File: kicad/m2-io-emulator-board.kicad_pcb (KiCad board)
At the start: 2 copper layers, 180 x 190 mm, 119 parts, among them J1 N2550-6002-RB, J10 61300811121, J11 61301011121, J12 Pin Header 02x18 2.54mm Verti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, J13 VGA femelle, J14 VIDEO, J2 N2526-6002-RB, J3 B10P-SHF-1AA, J4 B12P-SHF-1AA, J5 B12P-SHF-1AA, J6 61300811121, J7 61300811121, J8 61300811121, J9 61300811121, SW1 TEST, SW2 SERVICE, U2 74HCT86, U3 OPA3355EA

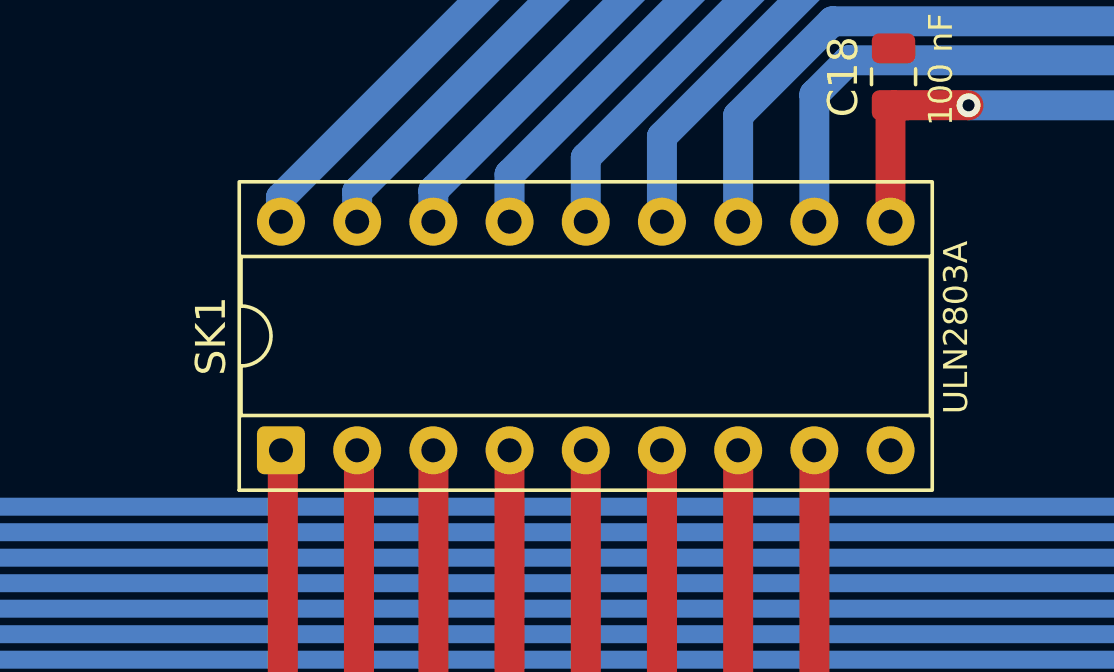
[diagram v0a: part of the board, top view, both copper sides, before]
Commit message: U1 (ULN2803A) soldered directly: DIP-18 socket SK1 removed from schematic, PCB and BOM; Gerbers (silkscreen only), schematic PDF and renders updated
Co-Authored-By: Claude Opus 5.5 <noreply@anthropic.com>
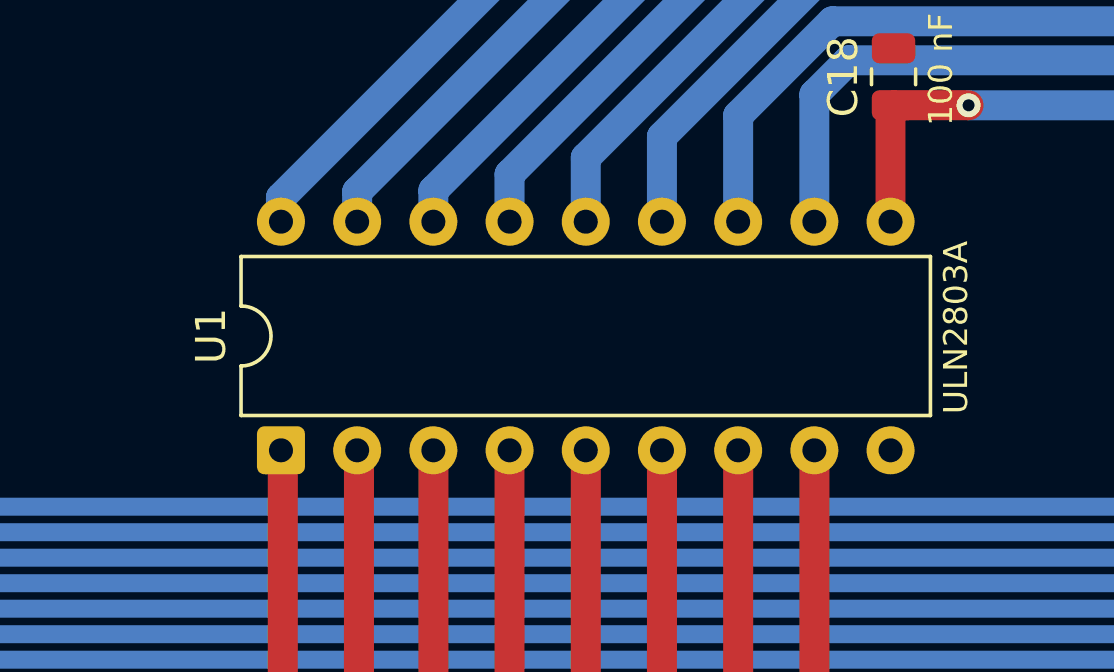
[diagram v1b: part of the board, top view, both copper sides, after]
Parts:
- removed SK1: 1-2199298-5, Package_DIP:DIP-18_W7.62mm_Socket
- added U1: ULN2803A, Package_DIP:DIP-18_W7.62mm, F.Cu at (68.7, 34.6)

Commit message: V2: screen jumper JP8 (Mega D36 to ground: ON = CRT 4:3, OFF = LVDS 16:9), framed silkscreen; Gerbers, drill files, schematic PDF, renders and BOM (EN/FR) updated
V1, the board ordered from JLCPCB on 2026-10-13, is tagged v1. JLCPCB BOM and CPL are unchanged (JP8 is through-hole).

Co-Authored-By: Claude Opus 5.5 <noreply@anthropic.com>
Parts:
- added JP8: 61300211121, Connector_PinHeader_2.54mm:PinHeader_1x02_P2.54mm_Vertical, F.Cu at (80.0, 118.0)
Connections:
- J12 pad 18: unconnected-(J12-Pin_17-Pad18) -> /MEGA_D36_ECRAN
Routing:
- net /MEGA_D36_ECRAN: track 0.00 -> 50.4 mm, vias 0 -> 1
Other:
- board text added: "OFF = LVDS 16:9"
- board text added: "ON = CRT (4:3)"
- board text added: "SCREEN"

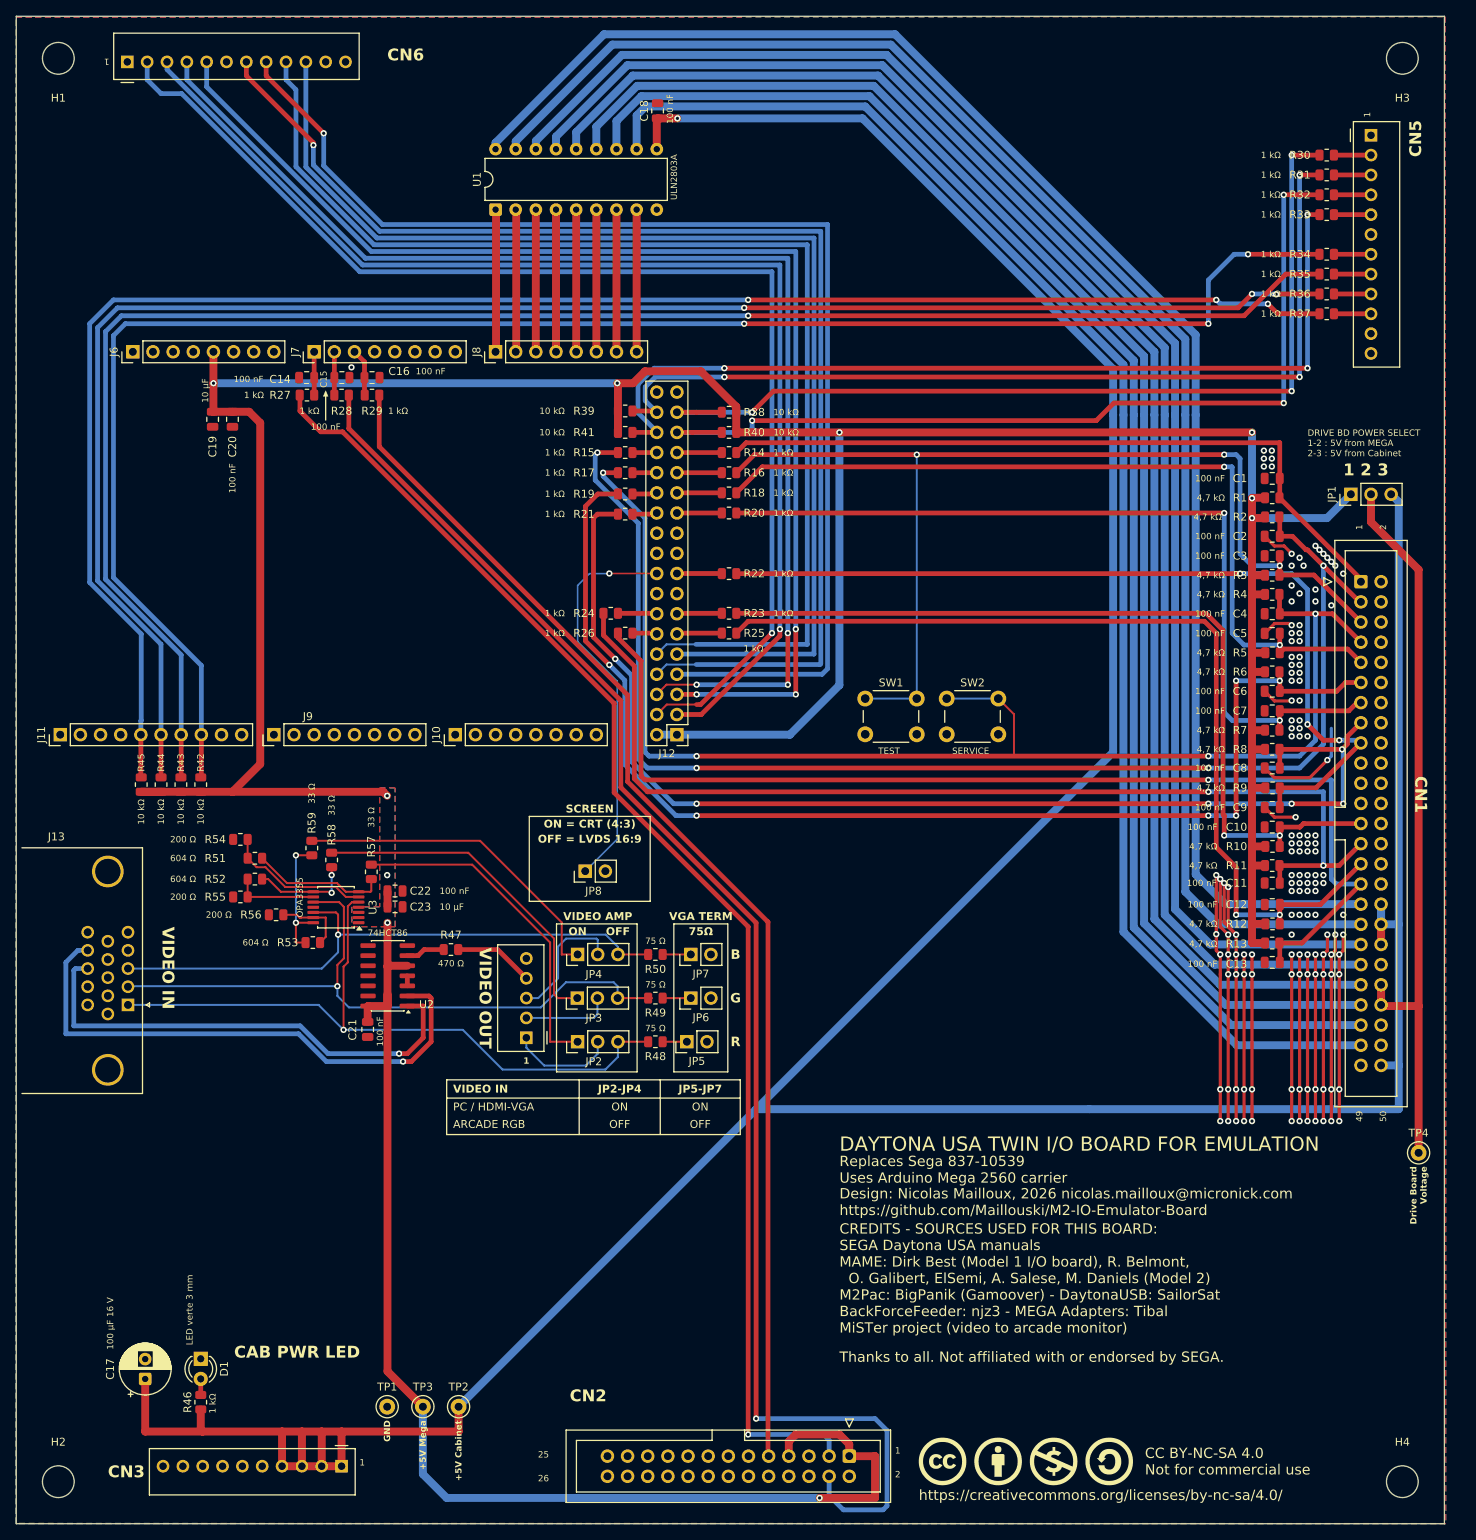
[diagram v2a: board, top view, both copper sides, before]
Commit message: V3: HDMI input with on-board HDMI to VGA converter (CS5213), source jumper JP9, converter power jumper JP10, stereo RCA output, optional EDID EEPROM (DNP); Gerbers, drill files, schematic PDF, renders, BOM (EN/FR) and JLCPCB files updated
Co-Authored-By: Claude Opus 5.5 <noreply@anthropic.com>
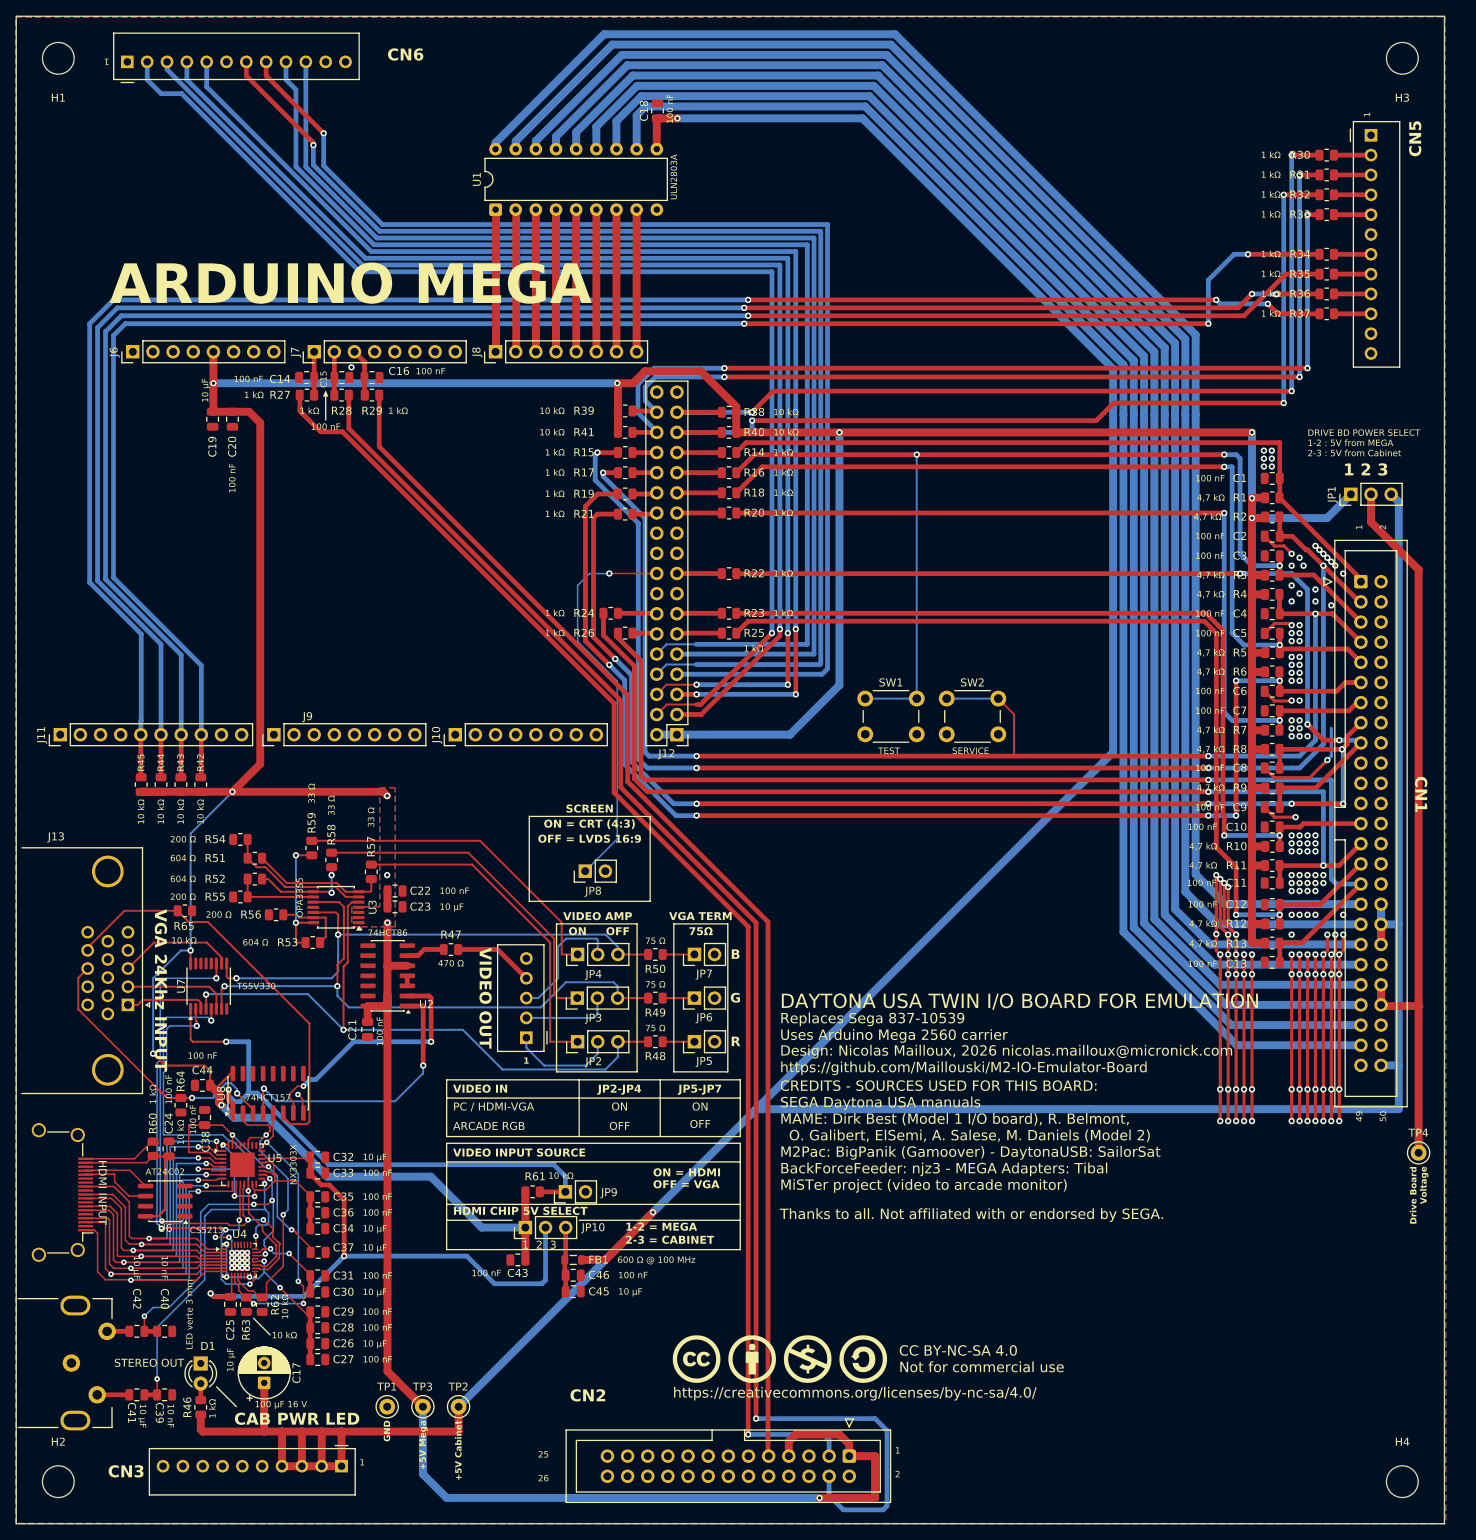
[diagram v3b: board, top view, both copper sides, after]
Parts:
- added C24: 100 nF, Capacitor_SMD:C_0805_2012Metric, F.Cu at (27.5, 153.0)
- added C25: 10 µF, Capacitor_SMD:C_0805_2012Metric, F.Cu at (35.2, 172.6)
- added C26: 10 µF, Capacitor_SMD:C_0805_2012Metric, F.Cu at (46.2, 177.6)
- added C27: 100 nF, Capacitor_SMD:C_0805_2012Metric, F.Cu at (46.2, 179.6)
- added C28: 100 nF, Capacitor_SMD:C_0805_2012Metric, F.Cu at (46.2, 175.6)
- added C29: 100 nF, Capacitor_SMD:C_0805_2012Metric, F.Cu at (46.2, 173.6)
- added C30: 10 µF, Capacitor_SMD:C_0805_2012Metric, F.Cu at (46.2, 171.1)
- added C31: 100 nF, Capacitor_SMD:C_0805_2012Metric, F.Cu at (46.2, 169.0)
- added C32: 10 µF, Capacitor_SMD:C_0805_2012Metric, F.Cu at (46.2, 154.1)
- added C33: 100 nF, Capacitor_SMD:C_0805_2012Metric, F.Cu at (46.2, 156.1)
- added C34: 10 µF, Capacitor_SMD:C_0805_2012Metric, F.Cu at (46.2, 163.1)
- added C35: 100 nF, Capacitor_SMD:C_0805_2012Metric, F.Cu at (46.2, 159.1)
- added C36: 100 nF, Capacitor_SMD:C_0805_2012Metric, F.Cu at (46.2, 161.1)
- added C37: 10 µF, Capacitor_SMD:C_0805_2012Metric, F.Cu at (46.3, 166.1)
- added C38: 100 nF, Capacitor_SMD:C_0805_2012Metric, F.Cu at (32.0, 149.1)
- added C39: 10 nF, Capacitor_SMD:C_0805_2012Metric, F.Cu at (26.9, 184.0)
- added C40: 10 nF, Capacitor_SMD:C_0805_2012Metric, F.Cu at (26.9, 176.0)
- added C41: 10 µF, Capacitor_SMD:C_0805_2012Metric, F.Cu at (23.4, 184.0)
- added C42: 10 µF, Capacitor_SMD:C_0805_2012Metric, F.Cu at (23.4, 176.0)
- added C43: 100 nF, Capacitor_SMD:C_0805_2012Metric, F.Cu at (71.5, 167.0)
- added C44: 100 nF, Capacitor_SMD:C_0805_2012Metric, F.Cu at (31.7, 145.0)
- added C45: 10 µF, Capacitor_SMD:C_0805_2012Metric, F.Cu at (78.5, 171.0)
- added C46: 100 nF, Capacitor_SMD:C_0805_2012Metric, F.Cu at (78.5, 168.9)
- added FB1: 600 Ω @ 100 MHz, Inductor_SMD:L_0805_2012Metric, F.Cu at (78.5, 167.0)
- added J15: HDMI A, Connector_Video:HDMI_A_Amphenol_10029449-x01xLF_Horizontal, F.Cu at (12.0, 158.5)
- added J16: RCJ-2223, interface-borne:CUI_RCJ-22xx_RCA_Dual_Horizontal, F.Cu at (8.20, 180.0)
- added JP10: 61300311121, Connector_PinHeader_2.54mm:PinHeader_1x03_P2.54mm_Vertical, F.Cu at (72.4, 162.9)
- added JP9: 61300211121, Connector_PinHeader_2.54mm:PinHeader_1x02_P2.54mm_Vertical, F.Cu at (77.5, 158.4)
- added R60: 1 kΩ, Resistor_SMD:R_0805_2012Metric, F.Cu at (25.5, 153.0)
- added R61: 10 kΩ, Resistor_SMD:R_0805_2012Metric, F.Cu at (73.3, 158.4)
- added R62: 10 kΩ, Resistor_SMD:R_0805_2012Metric, F.Cu at (39.2, 172.6)
- added R63: 10 kΩ, Resistor_SMD:R_0805_2012Metric, F.Cu at (37.2, 172.6)
- added R64: 10 kΩ, Resistor_SMD:R_0805_2012Metric, F.Cu at (29.0, 147.5)
- added R65: 10 kΩ, Resistor_SMD:R_0805_2012Metric, F.Cu at (29.5, 123.0)
- added U4: CS5213, Package_DFN_QFN:QFN-32-1EP_4x4mm_P0.4mm_EP2.65x2.65mm, F.Cu at (36.4, 167.1)
- added U5: NX3303X, Package_DFN_QFN:QFN-32-1EP_5x5mm_P0.5mm_EP3.1x3.1mm, F.Cu at (36.8, 155.0)
- added U6: AT24C02, Package_SO:SOIC-8_3.9x4.9mm_P1.27mm, F.Cu at (27.0, 159.6)
- added U7: TS5V330, Package_SO:TSSOP-16_4.4x5mm_P0.65mm, F.Cu at (32.5, 132.5)
- added U8: 74HCT157, Package_SO:SOIC-16_3.9x9.9mm_P1.27mm, F.Cu at (40.0, 146.0)
- moved LOGO1 33.6 mm to (91.0, 179.5)
- moved C17 15.0 mm to (39.5, 182.5)
- moved JP5 0.96 mm to (93.7, 139.5)
- moved R46 0.66 mm to (31.5, 185.6)
- moved D1 0.59 mm to (31.5, 180.0)
- moved JP6 0.46 mm to (93.7, 134.0)
- moved JP7 0.46 mm to (93.7, 128.5)
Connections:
- J13 pad 1: /VGA_R -> /J13_R
- J13 pad 13: /VGA_HS -> /J13_HS
- J13 pad 14: /VGA_VS -> /J13_VS
- J13 pad 2: /VGA_G -> /J13_G
- J13 pad 3: /VGA_B -> /J13_B
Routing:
- net /+5V_MEGA: track 557.0 -> 666.6 mm, vias 10 -> 14
- net /+5V_CONV: track 0.00 -> 77.2 mm, vias 0 -> 2
- net /SRC_SEL: track 0.00 -> 74.4 mm, vias 0 -> 2
- net /HD_B: track 0.00 -> 67.2 mm, vias 0 -> 5
- net /HD_G: track 0.00 -> 60.5 mm, vias 0 -> 4
- net /J13_VS: track 0.00 -> 52.8 mm
- net /HDMI_D2_N: track 0.00 -> 50.1 mm, vias 0 -> 2
- net /HD_R: track 0.00 -> 48.8 mm, vias 0 -> 2
- net /HDMI_D2_P: track 0.00 -> 48.3 mm, vias 0 -> 2
- net /HDMI_D1_N: track 0.00 -> 47.1 mm, vias 0 -> 2
- net /HDMI_D0_N: track 0.00 -> 46.6 mm, vias 0 -> 2
- net /HDMI_D1_P: track 0.00 -> 46.3 mm, vias 0 -> 2
- net /HDMI_CK_N: track 0.00 -> 45.9 mm, vias 0 -> 2
- net /HDMI_CK_P: track 0.00 -> 45.9 mm, vias 0 -> 2
- net /HDMI_D0_P: track 0.00 -> 45.5 mm, vias 0 -> 2
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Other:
- board text added: "1-2 = MEGA"
- board text added: "2-3 = CABINET"
- board text added: "ARDUINO MEGA"
- board text added: "HDMI CHIP 5V SELECT"
- board text added: "OFF = VGA"
- board text added: "ON = HDMI"
- board text added: "VGA 24Khz INPUT"
- board text added: "VIDEO INPUT SOURCE"
